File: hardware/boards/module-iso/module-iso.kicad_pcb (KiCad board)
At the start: 2 copper layers, 48.5 x 46.2 mm, 11 parts, among them J1 2x5 2.54mm pin header, U14 RPA20-2412SAW

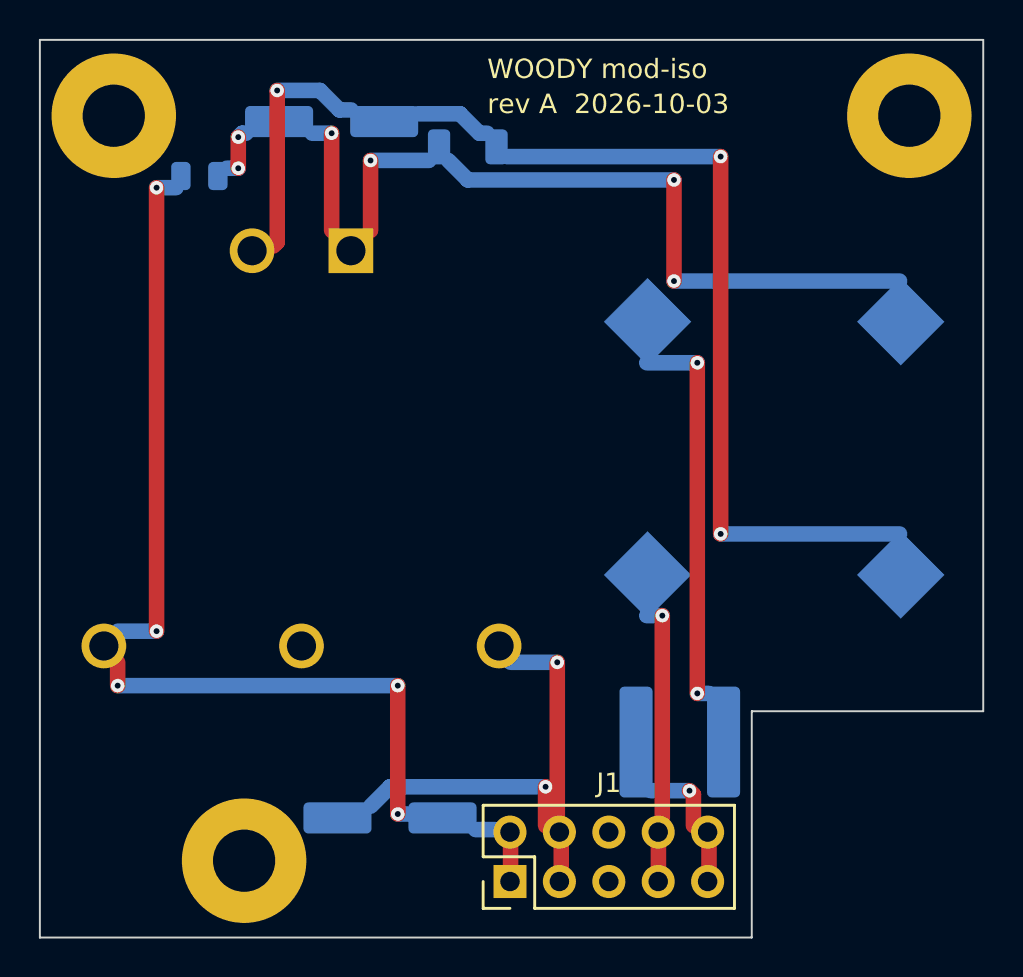
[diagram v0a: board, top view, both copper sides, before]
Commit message: module-main placed for the iso board: U-ISO and its filter gone, J-B2B-ISO (J5) and three iso standoffs in; parts the new holes displaced re-placed (#22)
Co-Authored-By: Claude Opus 5.5 <noreply@anthropic.com>
Claude-Session: https://claude.ai/code/session_01LmB4muFXnoLprWX4JzuJ5A
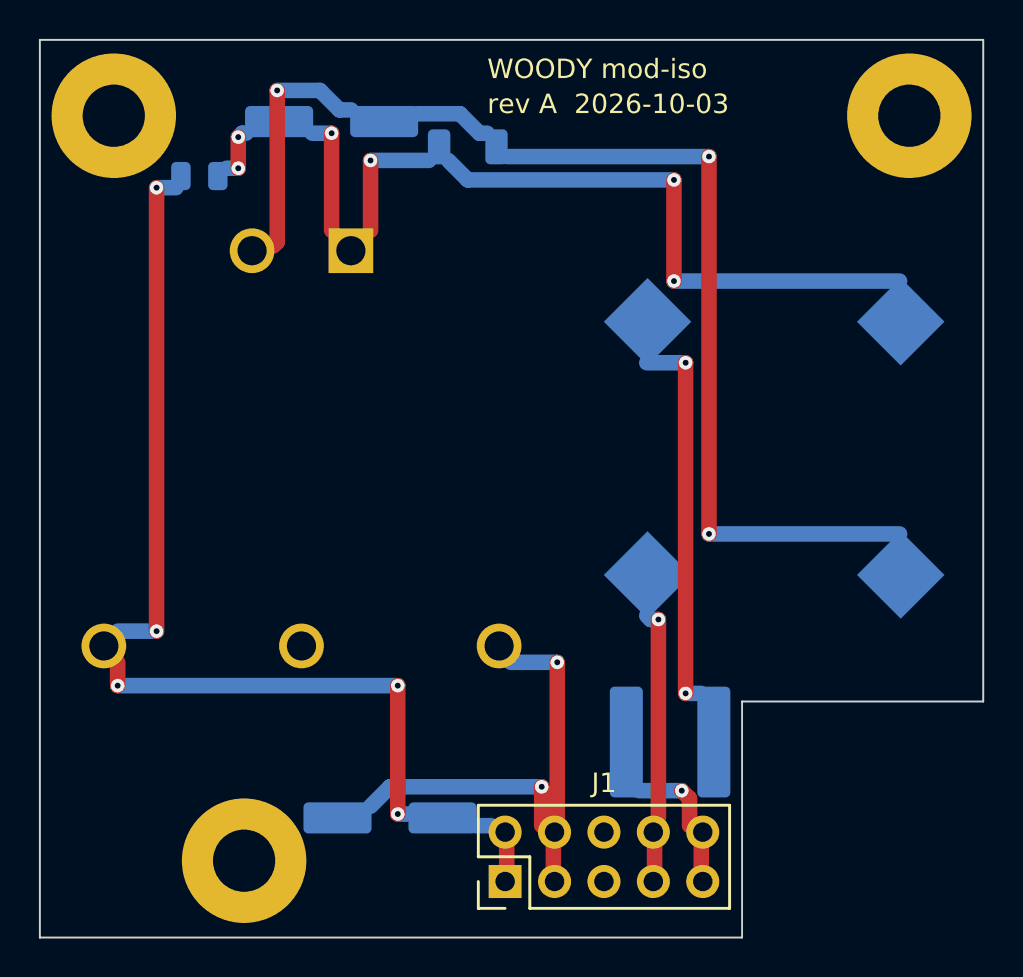
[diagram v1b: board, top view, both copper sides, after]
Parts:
- moved L1 0.50 mm to (93.4, 102.1)
- moved J1 0.25 mm to (84.9, 109.3)
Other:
- outline, holes or cut-outs redrawn

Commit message: module-iso: a power layout, placed and drawn by hand (owner review); two iso standoffs, not three (#22)
The iso board's copper is drawn, not autorouted: pours on both faces per region
(PWR_GND, ISO_VIN_NEG, ISO_FILT_NEG), stitched; supply runs straight with
45-degree bends, 1.2-1.5 mm; the 2 mm barrier across U-ISO's middle and past
J-B2B-ISO's open pair. pcb.py check passes on module-iso. The top-left iso
standoff is dropped (it stood in the breath pair's corridor on module-main):
two at opposite corners, MECH-STANDOFF-ISO 2, screws 10. J-B2B-ISO's 3D model
on both boards (setup-env fetches the 2x5).

Gate-Red: module-main is mid re-route for the iso board split (#22) - its pcb check, and the CAD outputs the body branch left stale, fail until it lands
Co-Authored-By: Claude Opus 5.5 <noreply@anthropic.com>
Claude-Session: https://claude.ai/code/session_01LmB4muFXnoLprWX4JzuJ5A
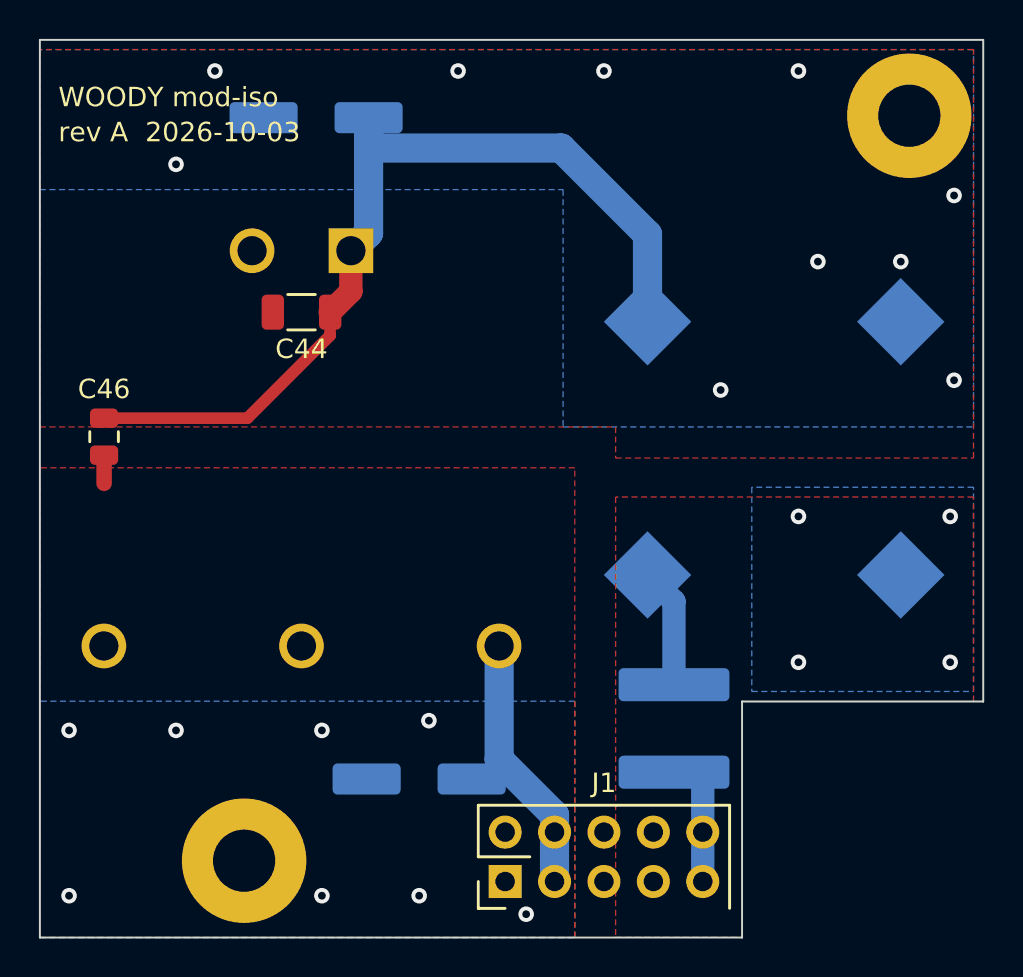
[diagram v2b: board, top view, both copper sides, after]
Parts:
- removed H3: MECH-STANDOFF-ISO 3, MountingHole:MountingHole_3.2mm_M3_Pad
- C44, C46: moved to F.Cu
- moved H2 40.9 mm to (105.7, 69.9)
- moved C46 14.3 mm to (64.3, 86.4), turned to -90 degrees
- moved C44 12.1 mm to (74.5, 80.0), turned to 180 degrees
- moved C45 2.50 mm to (80.5, 104.0), turned to 180 degrees
- moved C2 0.82 mm to (75.2, 70.0), turned to 180 degrees
- moved L1 0.73 mm to (93.6, 101.4), turned to 90 degrees
- turned L2 to 135 degrees
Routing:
- net /power-entry/ISO_VIN_NEG: track 55.9 -> 0.00 mm, vias 3 -> 10
- net /PWR_GND: track 50.6 -> 1.45 mm, vias 5 -> 8
- net /power-entry/ISO_FILT_POS: track 19.8 -> 6.20 mm, vias 2 -> 0
- net /ISO_FILT_NEG: track 12.1 -> 0.00 mm, vias 1 -> 4
- net /ISO_POS12: track 22.8 -> 13.3 mm, vias 2 -> 0
- net /power-entry/ISO_VIN_POS: track 44.1 -> 46.1 mm, vias 6 -> 0
- net /ISO_FB2: track 5.37 -> 5.62 mm, vias 1 -> 0
- added copper zone on B.Cu, net /ISO_FILT_NEG
- added copper zone on F.Cu, net /ISO_FILT_NEG
- added copper zone on B.Cu, net /PWR_GND
- added copper zone on F.Cu, net /PWR_GND
- added copper zone on B.Cu, net /power-entry/ISO_VIN_NEG
- added copper zone on F.Cu, net /power-entry/ISO_VIN_NEG
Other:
- board text added: "C2"
- board text removed: "C45"
